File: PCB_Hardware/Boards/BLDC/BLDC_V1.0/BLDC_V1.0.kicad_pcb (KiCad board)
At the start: 4 copper layers, 0 parts

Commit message: Created organization around the symbol lib and did a first pass layout of the BDLC
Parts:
- added C1: 100n, Capacitor_SMD:C_0402_1005Metric, B.Cu at (191.8, 98.6)
- added C11: 33n, Capacitor_SMD:C_0402_1005Metric, B.Cu at (172.3, 99.6)
- added C12: 1u, Capacitor_SMD:C_0603_1608Metric, F.Cu at (181.4, 90.2)
- added C13: 100n, Capacitor_SMD:C_0402_1005Metric, F.Cu at (175.8, 90.4)
- added C14: 10u, Capacitor_SMD:C_0603_1608Metric, F.Cu at (177.4, 115.6)
- added C15: 1u, Capacitor_SMD:C_0603_1608Metric, F.Cu at (194.4, 97.0)
- added C16: 47n, Capacitor_SMD:C_0805_2012Metric, F.Cu at (191.0, 96.8)
- added C17: 100n, Capacitor_SMD:C_0402_1005Metric, F.Cu at (193.0, 94.8)
- added C18: 1u, Capacitor_SMD:C_0402_1005Metric, F.Cu at (189.6, 96.0)
- added C19: 1u, Capacitor_SMD:C_0402_1005Metric, F.Cu at (187.8, 96.2)
- added C2: 100n, Capacitor_SMD:C_0402_1005Metric, B.Cu at (167.0, 94.9)
- added C20: 1u, Capacitor_SMD:C_0402_1005Metric, F.Cu at (185.8, 84.5)
- added C21: 100n, Capacitor_SMD:C_0402_1005Metric, F.Cu at (186.5, 85.2)
- added C22: 2.2u, Capacitor_SMD:C_0805_2012Metric, F.Cu at (202.1, 88.5)
- added C23: 330u, Capacitor_THT:CP_Radial_D12.5mm_P5.00mm, F.Cu at (193.0, 107.6)
- added C24: 10u, Capacitor_SMD:C_0603_1608Metric, B.Cu at (168.8, 107.0)
- added C25: 2.2u, Capacitor_SMD:C_0805_2012Metric, F.Cu at (202.3, 74.5)
- added C26: 2.2u, Capacitor_SMD:C_0805_2012Metric, F.Cu at (202.2, 102.2)
- added C28: 100n, Capacitor_SMD:C_0805_2012Metric, F.Cu at (185.4, 97.4)
- added C29: 100n, Capacitor_SMD:C_0402_1005Metric, B.Cu at (179.2, 84.8)
- added C3: 100n, Capacitor_SMD:C_0402_1005Metric, F.Cu at (167.0, 85.9)
- added C30: 4.7u, Capacitor_SMD:C_0603_1608Metric, B.Cu at (203.8, 80.2)
- added C31: 100n, Capacitor_SMD:C_0402_1005Metric, B.Cu at (203.0, 77.6)
- added C32: 100n, Capacitor_SMD:C_0402_1005Metric, B.Cu at (192.8, 71.8)
- added C33: 100n, Capacitor_SMD:C_0402_1005Metric, B.Cu at (187.0, 82.4)
- added C34: 100n, Capacitor_SMD:C_0402_1005Metric, B.Cu at (190.0, 88.8)
- added C35: 100n, Capacitor_SMD:C_0402_1005Metric, B.Cu at (196.2, 88.2)
- added C36: 100n, Capacitor_SMD:C_0402_1005Metric, B.Cu at (191.0, 73.6)
- added C37: 4.7u, Capacitor_SMD:C_0603_1608Metric, F.Cu at (199.8, 70.2)
- added C38: 100n, Capacitor_SMD:C_0402_1005Metric, F.Cu at (207.6, 72.4)
- added C39: 10u, Capacitor_SMD:C_0402_1005Metric, B.Cu at (190.0, 116.8)
- added C4: 47n, Capacitor_SMD:C_0402_1005Metric, F.Cu at (176.4, 86.8)
- added C40: 22u, Capacitor_SMD:C_0805_2012Metric, B.Cu at (187.3, 122.3)
- added C41: 22u, Capacitor_SMD:C_0805_2012Metric, F.Cu at (188.2, 113.5)
- added C42: 100n, Capacitor_SMD:C_0402_1005Metric, B.Cu at (190.2, 72.8)
- added C43: 18p, Capacitor_SMD:C_0402_1005Metric, B.Cu at (185.2, 89.9)
- added C44: 18p, Capacitor_SMD:C_0402_1005Metric, B.Cu at (185.2, 84.4)
- added C45: 100n, Capacitor_SMD:C_0402_1005Metric, B.Cu at (182.6, 91.0)
- added C46: 100n, Capacitor_SMD:C_0402_1005Metric, F.Cu at (201.2, 90.0)
- added C47: ?, Capacitor_SMD:C_0402_1005Metric, F.Cu at (193.4, 77.8)
- added C48: ?, Capacitor_SMD:C_0402_1005Metric, F.Cu at (195.6, 77.8)
- added C49: ?, Capacitor_SMD:C_0402_1005Metric, F.Cu at (197.8, 77.8)
- added C50: 2.2u, Capacitor_SMD:C_0805_2012Metric, B.Cu at (168.8, 117.4)
- added C51: 2.2n, Capacitor_SMD:C_0402_1005Metric, B.Cu at (178.2, 121.2)
- added C52: 3.3n, Capacitor_SMD:C_0402_1005Metric, B.Cu at (181.2, 121.2)
- added C53: 56p, Capacitor_SMD:C_0402_1005Metric, B.Cu at (182.4, 121.2)
- added C54: 22u, Capacitor_SMD:C_0805_2012Metric, B.Cu at (184.2, 116.4)
- added C57: 100n, Capacitor_SMD:C_0402_1005Metric, B.Cu at (212.2, 122.2)
- added D1: SD05T1G, Diode_SMD:D_SOD-323, B.Cu at (194.0, 97.4)
- added D10: SMAJ5.0A, Diode_SMD:D_SMA, B.Cu at (196.8, 66.0)
- added D11: RED, LED_SMD:LED_0603_1608Metric, F.Cu at (218.4, 115.6)
- added D12: RED, LED_SMD:LED_0603_1608Metric, F.Cu at (218.4, 113.8)
- added D13: RED, LED_SMD:LED_0603_1608Metric, F.Cu at (171.8, 85.6)
- added D14: PESD5V0L1UL, Diode_SMD:D_SOD-882, B.Cu at (197.6, 68.6)
- added D15: SMCJ90A, Diode_SMD:D_SMC, B.Cu at (207.8, 105.8)
- added D16: SMCJ90A, Diode_SMD:D_SMC, B.Cu at (207.8, 99.0)
- added D17: SMCJ90A, Diode_SMD:D_SMC, B.Cu at (214.8, 75.1)
- added D18: BZG05C75-M3-08, Diode_SMD:D_SMA, B.Cu at (166.1, 109.0)
- added D19: PESD5V0L1UL, Diode_SMD:D_SOD-882, F.Cu at (168.8, 71.3)
- added D2: PESD1CAN, Package_TO_SOT_SMD:SOT-23, F.Cu at (176.4, 78.8)
- added D20: PESD5V0L1UL, Diode_SMD:D_SOD-882, F.Cu at (170.2, 71.3)
- added D21: RED, LED_SMD:LED_0603_1608Metric, F.Cu at (168.2, 122.2)
- added D22: PESD5V0S1UL, Diode_SMD:D_SOD-882, B.Cu at (209.8, 122.0)
- added D23: PESD3V3S1UL, Diode_SMD:D_SOD-882, B.Cu at (207.2, 122.0)
- added D24: PESD5V0S1UL, Diode_SMD:D_SOD-882, B.Cu at (204.8, 122.0)
- added D3: PESD1CAN, Package_TO_SOT_SMD:SOT-23, B.Cu at (173.0, 80.8)
- added D4: SMCJ78A, Diode_SMD:D_SMC, F.Cu at (174.0, 120.0)
- added D5: SS10150, Diode_SMD:D_SOD-123F, B.Cu at (196.0, 113.8)
- added D6: PESD3V3S1UL, Diode_SMD:D_SOD-882, B.Cu at (181.4, 70.0)
- added D7: PESD5V0L1UL, Diode_SMD:D_SOD-882, B.Cu at (185.8, 73.8)
- added D8: PESD3V3S1UL, Diode_SMD:D_SOD-882, B.Cu at (182.0, 72.0)
- added D9: PESD3V3S1UL, Diode_SMD:D_SOD-882, B.Cu at (176.6, 70.0)
- added F1: MF-PSMF050X-2, Fuse:Fuse_0805_2012Metric, B.Cu at (185.8, 76.4)
- added F2: MF-PSMF050X-2, Fuse:Fuse_0805_2012Metric, B.Cu at (184.0, 71.0)
- added F3: MF-PSMF050X-2, Fuse:Fuse_0805_2012Metric, F.Cu at (169.4, 65.4)
- added F4: MF-PSMF050X-2, Fuse:Fuse_0805_2012Metric, F.Cu at (195.0, 71.4)
- added F5: MF-PSMF050X-2, Fuse:Fuse_0805_2012Metric, B.Cu at (186.6, 68.8)
- added F6: MF-PSMF050X-2, Fuse:Fuse_1812_4532Metric, B.Cu at (201.4, 115.4)
- added H1: MountingHole, MountingHole:MountingHole_3.2mm_M3, F.Cu at (164.0, 68.0)
- added H2: MountingHole, MountingHole:MountingHole_3.2mm_M3, F.Cu at (164.0, 120.0)
- added H3: MountingHole, MountingHole:MountingHole_3.2mm_M3, F.Cu at (216.0, 120.0)
- added H4: MountingHole, MountingHole:MountingHole_3.2mm_M3, F.Cu at (216.0, 68.0)
- added H5: MountingHole_Pad, MountingHole:MountingHole_3.2mm_M3_DIN965_Pad, F.Cu at (216.2, 105.9)
- added H6: MountingHole_Pad, MountingHole:MountingHole_3.2mm_M3_DIN965_Pad, F.Cu at (215.9, 94.2)
- added H7: MountingHole_Pad, MountingHole:MountingHole_3.2mm_M3_DIN965_Pad, F.Cu at (215.7, 82.3)
- added J1: Conn_01x04_Pin, DBRobot:CONN_JST_SM04B-PASS, B.Cu at (165.0, 78.8)
- added J11: GT-USB-7010ASV, Connector_USB:USB_C_Receptacle_G-Switch_GT-USB-7010ASV, F.Cu at (206.0, 67.0)
- added J14: 47053-1000, Connector:FanPinHeader_1x04_P2.54mm_Vertical, F.Cu at (202.2, 119.7)
- added J2: Conn_01x04_Pin, DBRobot:CONN_JST_SM04B-PASS, F.Cu at (165.0, 78.8)
- added J3: Conn_01x02_Pin, Connector_AMASS:AMASS_XT30PW-M_1x02_P2.50mm_Horizontal, F.Cu at (173.0, 106.5)
- added J4: Conn_01x02_Pin, Connector_AMASS:AMASS_XT30PW-M_1x02_P2.50mm_Horizontal, F.Cu at (173.0, 91.2)
- added J5: Conn_01x02_Socket, Connector_JST:JST_XH_S2B-XH-A-1_1x02_P2.50mm_Horizontal, F.Cu at (194.8, 116.2)
- added J6: Conn_01x02_Socket, Connector_JST:JST_GH_SM02B-GHS-TB_1x02-1MP_P1.25mm_Horizontal, B.Cu at (179.0, 67.0)
- added J7: Conn_ARM_SWD_TagConnect_TC2030, Connector:Tag-Connect_TC2030-IDC-FP_2x03_P1.27mm_Vertical, F.Cu at (180.5, 96.2)
- added J8: Conn_02x06_Odd_Even, Connector_JST:JST_PUD_S12B-PUDSS-1_2x06_P2.00mm_Horizontal, F.Cu at (184.0, 75.8)
- added J9: Conn_01x06_Socket, Connector_JST:JST_GH_SM06B-GHS-TB_1x06-1MP_P1.25mm_Horizontal, F.Cu at (193.0, 67.0)
- added L1: 68u SRN5040TA-680K, Inductor_SMD:L_Sunlord_SWPA4020S, B.Cu at (180.6, 117.8)
- added Q1: SI2302, Package_TO_SOT_SMD:SOT-23, F.Cu at (173.8, 81.8)
- added Q10: BC847, Package_TO_SOT_SMD:SOT-23, B.Cu at (190.2, 120.4)
- added Q11: BSS138, Package_TO_SOT_SMD:SOT-23, B.Cu at (211.4, 117.4)
- added Q12: BSS84, Package_TO_SOT_SMD:SOT-23, B.Cu at (180.6, 79.4)
- added Q13: IPT015N10N5, Package_TO_SOT_SMD:Infineon_PG-HSOF-8-1, B.Cu at (181.0, 107.6)
- added Q14: SI2302, Package_TO_SOT_SMD:SOT-23, B.Cu at (169.6, 69.4)
- added Q2: IPT015N10N5, Package_TO_SOT_SMD:Infineon_PG-HSOF-8-1, F.Cu at (181.0, 107.5)
- added Q3: TPH3R70APL, DBRobot:SOP AdvanceN_TOS, F.Cu at (208.3, 104.4)
- added Q4: TPH3R70APL, DBRobot:SOP AdvanceN_TOS, F.Cu at (208.3, 111.4)
- added Q5: TPH3R70APL, DBRobot:SOP AdvanceN_TOS, F.Cu at (208.3, 90.5)
- added Q6: TPH3R70APL, DBRobot:SOP AdvanceN_TOS, F.Cu at (208.3, 97.5)
- added Q7: TPH3R70APL, DBRobot:SOP AdvanceN_TOS, F.Cu at (208.4, 76.5)
- added Q8: TPH3R70APL, DBRobot:SOP AdvanceN_TOS, F.Cu at (208.4, 83.4)
- added Q9: TPH3R70APL, DBRobot:SOP AdvanceN_TOS, B.Cu at (197.2, 120.6)
- added R1: 60, Resistor_SMD:R_0805_2012Metric, F.Cu at (176.6, 82.4)
- added R10: 3.9k, Resistor_SMD:R_0805_2012Metric, B.Cu at (170.1, 98.3)
- added R11: 3.9k, Resistor_SMD:R_0402_1005Metric, B.Cu at (176.0, 99.5)
- added R12: 1m, Resistor_SMD:R_2512_6332Metric, F.Cu at (202.4, 107.2)
- added R13: 1m, Resistor_SMD:R_2512_6332Metric, F.Cu at (202.3, 94.4)
- added R14: 1m, Resistor_SMD:R_2512_6332Metric, F.Cu at (202.1, 79.6)
- added R15: 1k, Resistor_SMD:R_0402_1005Metric, F.Cu at (186.6, 81.9)
- added R16: 1k, Resistor_SMD:R_0402_1005Metric, F.Cu at (188.3, 79.7)
- added R17: 100k, Resistor_SMD:R_0603_1608Metric, B.Cu at (177.0, 86.2)
- added R18: 10k, Resistor_SMD:R_0402_1005Metric, B.Cu at (187.6, 120.2)
- added R19: 4.7, Resistor_SMD:R_0402_1005Metric, B.Cu at (190.2, 122.8)
- added R2: 60, Resistor_SMD:R_0805_2012Metric, F.Cu at (175.8, 85.2)
- added R20: 1k, Resistor_SMD:R_0402_1005Metric, B.Cu at (188.8, 118.8)
- added R21: 4.7k, Resistor_SMD:R_0603_1608Metric, B.Cu at (177.0, 84.6)
- added R22: 10k, Resistor_SMD:R_0402_1005Metric, B.Cu at (209.0, 94.0)
- added R23: 10k, Resistor_SMD:R_0402_1005Metric, B.Cu at (179.4, 70.8)
- added R24: 0, Resistor_SMD:R_0402_1005Metric, B.Cu at (187.6, 87.8)
- added R25: 4.7k, Resistor_SMD:R_0402_1005Metric, B.Cu at (176.0, 78.0)
- added R26: 4.7k, Resistor_SMD:R_0402_1005Metric, B.Cu at (178.0, 78.0)
- added R27: 4.7k, Resistor_SMD:R_0402_1005Metric, F.Cu at (195.0, 84.4)
- added R28: 4.7k, Resistor_SMD:R_0402_1005Metric, F.Cu at (199.6, 89.2)
- added R29: 49, Resistor_SMD:R_0805_2012Metric, B.Cu at (166.1, 103.3)
- added R30: 24.9k, Resistor_SMD:R_0402_1005Metric, B.Cu at (170.8, 116.0)
- added R31: 121k, Resistor_SMD:R_0402_1005Metric, B.Cu at (180.0, 121.2)
- added R32: 0, Resistor_SMD:R_0402_1005Metric, F.Cu at (196.7, 77.8)
- added R33: 1.8k, Resistor_SMD:R_0402_1005Metric, F.Cu at (167.4, 71.1)
- added R34: 3.3k, Resistor_SMD:R_0402_1005Metric, F.Cu at (168.2, 68.6)
- added R35: 10k, Resistor_SMD:R_0402_1005Metric, B.Cu at (168.0, 67.8)
- added R36: 1k, Resistor_SMD:R_0402_1005Metric, B.Cu at (167.4, 71.1)
- added R37: 0, Resistor_SMD:R_0402_1005Metric, F.Cu at (194.5, 77.8)
- added R38: 0, Resistor_SMD:R_0402_1005Metric, F.Cu at (192.3, 77.8)
- added R39: 453k, Resistor_SMD:R_0402_1005Metric, B.Cu at (177.0, 116.0)
- added R40: 143k, Resistor_SMD:R_0402_1005Metric, B.Cu at (175.0, 116.0)
- added R47: 5.1k, Resistor_SMD:R_0402_1005Metric, B.Cu at (208.4, 68.2)
- added R48: 5.1k, Resistor_SMD:R_0402_1005Metric, B.Cu at (203.6, 68.2)
- added R49: 100k, Resistor_SMD:R_0402_1005Metric, B.Cu at (191.4, 117.7)
- added R50: 5k, Resistor_SMD:R_0402_1005Metric, B.Cu at (219.0, 117.0)
- added R51: 2.2k, Resistor_SMD:R_0402_1005Metric, B.Cu at (218.4, 113.8)
- added R52: 100k, Resistor_SMD:R_0402_1005Metric, B.Cu at (193.2, 116.0)
- added R53: 100k, Resistor_SMD:R_0402_1005Metric, B.Cu at (187.6, 113.8)
- added R54: 100k, Resistor_SMD:R_0402_1005Metric, B.Cu at (193.2, 114.0)
- added R55: 2.2k, Resistor_SMD:R_0402_1005Metric, F.Cu at (169.9, 85.9)
- added R56: 100, Resistor_SMD:R_0402_1005Metric, B.Cu at (208.8, 115.8)
- added R57: 100k, Resistor_SMD:R_0402_1005Metric, B.Cu at (209.0, 117.4)
- added R58: 10k, Resistor_SMD:R_0402_1005Metric, B.Cu at (211.2, 122.2)
- added R59: 10k, Resistor_SMD:R_0402_1005Metric, B.Cu at (205.4, 116.6)
- added R6: 0.5m, Resistor_SMD:R_2512_6332Metric, F.Cu at (181.4, 119.4)
- added R60: 1k, Resistor_SMD:R_0402_1005Metric, B.Cu at (205.4, 117.8)
- added R61: 2.2k, Resistor_SMD:R_0402_1005Metric, B.Cu at (168.2, 122.2)
- added R7: 102k, Resistor_SMD:R_0805_2012Metric, B.Cu at (166.0, 99.0)
- added R8: 30k, Resistor_SMD:R_0805_2012Metric, B.Cu at (163.2, 101.2)
- added R9: 113k, Resistor_SMD:R_0805_2012Metric, B.Cu at (168.0, 99.0)
- added TH1: Thermistor, Resistor_SMD:R_0603_1608Metric, B.Cu at (207.6, 94.0)
- added U1: DRV8353SRTAR, Package_DFN_QFN:QFN-40-1EP_6x6mm_P0.5mm_EP4.6x4.6mm, F.Cu at (190.4, 90.6)
- added U10: TPD2E2U06DCK, Package_TO_SOT_SMD:SOT-323_SC-70, B.Cu at (206.1, 65.6)
- added U11: AMS1117-3.3, Package_TO_SOT_SMD:SOT-223-3_TabPin2, F.Cu at (187.3, 119.1)
- added U12: LM66100DCK, Package_TO_SOT_SMD:SOT-363_SC-70-6, B.Cu at (187.3, 115.6)
- added U13: LM66100DCK, Package_TO_SOT_SMD:SOT-363_SC-70-6, B.Cu at (191.5, 114.2)
- added U14: SRV05-4, Package_TO_SOT_SMD:SOT-23-6, F.Cu at (188.8, 72.0)
- added U15: TS5A3159ADBVR, Package_TO_SOT_SMD:SOT-23-6, B.Cu at (189.8, 66.4)
- added U16: CAT24C512C8UTR, DBRobot:CAT24C512C8UTR, B.Cu at (200.3, 86.8)
- added U2: MT6835GT-STD, Package_SO:TSSOP-16_4.4x5mm_P0.65mm, B.Cu at (190.1, 94.0)
- added U3: TCAN1044VDR, Package_SO:SOIC-8_3.9x4.9mm_P1.27mm, B.Cu at (167.0, 90.6)
- added U4: ~, Package_SO:SOIC-8-1EP_3.9x4.9mm_P1.27mm_EP2.29x3mm, B.Cu at (173.8, 119.3)
- added U5: LM5069MM-2, Package_SO:MSOP-10_3x3mm_P0.5mm, B.Cu at (172.2, 101.9)
- added U6: TLV70233_SOT23-5, Package_TO_SOT_SMD:SOT-23-5, F.Cu at (178.4, 89.8)
- added U7: STM32G474RET6, Package_QFP:LQFP-64_10x10mm_P0.5mm, B.Cu at (195.0, 80.0)
- added U8: SRV05-4, Package_TO_SOT_SMD:SOT-23-6, F.Cu at (182.8, 78.8)
- added U9: SRV05-4, Package_TO_SOT_SMD:SOT-23-6, B.Cu at (173.6, 70.6)
- added Y2: XXGBBCNANF-25.000000MHZ, Crystal:Crystal_SMD_3225-4Pin_3.2x2.5mm, B.Cu at (185.2, 87.2)
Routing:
- net GND: track 0.00 -> 205.9 mm, vias 0 -> 91
- net +5V: track 0.00 -> 176.9 mm, vias 0 -> 6
- net /Break R/BREAK_R: track 0.00 -> 127.4 mm, vias 0 -> 11
- net /OR Inputs/5V_USB: track 0.00 -> 103.8 mm, vias 0 -> 6
- net +3.3V: track 0.00 -> 81.6 mm, vias 0 -> 18
- net +BATT: track 0.00 -> 77.6 mm, vias 0 -> 66
- net /Encoder/ENCODER_MOSI: track 0.00 -> 70.5 mm, vias 0 -> 2
- net /Encoder/ENCODER_MISO: track 0.00 -> 64.0 mm, vias 0 -> 4
- net /CANFD/CAN-: track 0.00 -> 60.9 mm, vias 0 -> 2
- net /CANFD/CAN+: track 0.00 -> 58.7 mm, vias 0 -> 2
- net /MCU/SWDIO: track 0.00 -> 47.8 mm, vias 0 -> 4
- net /GPIO/AUX2_V_CRTL: track 0.00 -> 46.4 mm, vias 0 -> 3
- net +3.3VA: track 0.00 -> 46.4 mm, vias 0 -> 3
- net /GPIO/PA8/SDA: track 0.00 -> 44.8 mm, vias 0 -> 1
- net /Fan/TACH: track 0.00 -> 44.8 mm, vias 0 -> 2
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- added copper zone on F.Cu, net +12-60V
- added copper zone on In2.Cu, net +3.3V
- added copper zone on B.Cu, net +BATT
- added copper zone on In2.Cu, net +BATT
- added copper zone on In1.Cu, net GND
- added copper zone on B.Cu, net Net-(D15-K)
- added copper zone on F.Cu, net Net-(D15-K)
- added copper zone on B.Cu, net Net-(D16-K)
- added copper zone on F.Cu, net Net-(D16-K)
- added copper zone on B.Cu, net Net-(D17-K)
- added copper zone on F.Cu, net Net-(D17-K)
- added copper zone on B.Cu, net Net-(D18-K)
- added copper zone on B.Cu, net Net-(Q13-S)
- added copper zone on F.Cu, net Net-(Q13-S)
- added copper zone on F.Cu, net Net-(Q2-D)
- added copper zone on F.Cu, net Net-(U1-SPA)
- added copper zone on F.Cu, net Net-(U1-SPB)
- added copper zone on F.Cu, net Net-(U1-SPC)
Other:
- board outline added: 60 x 60 mm

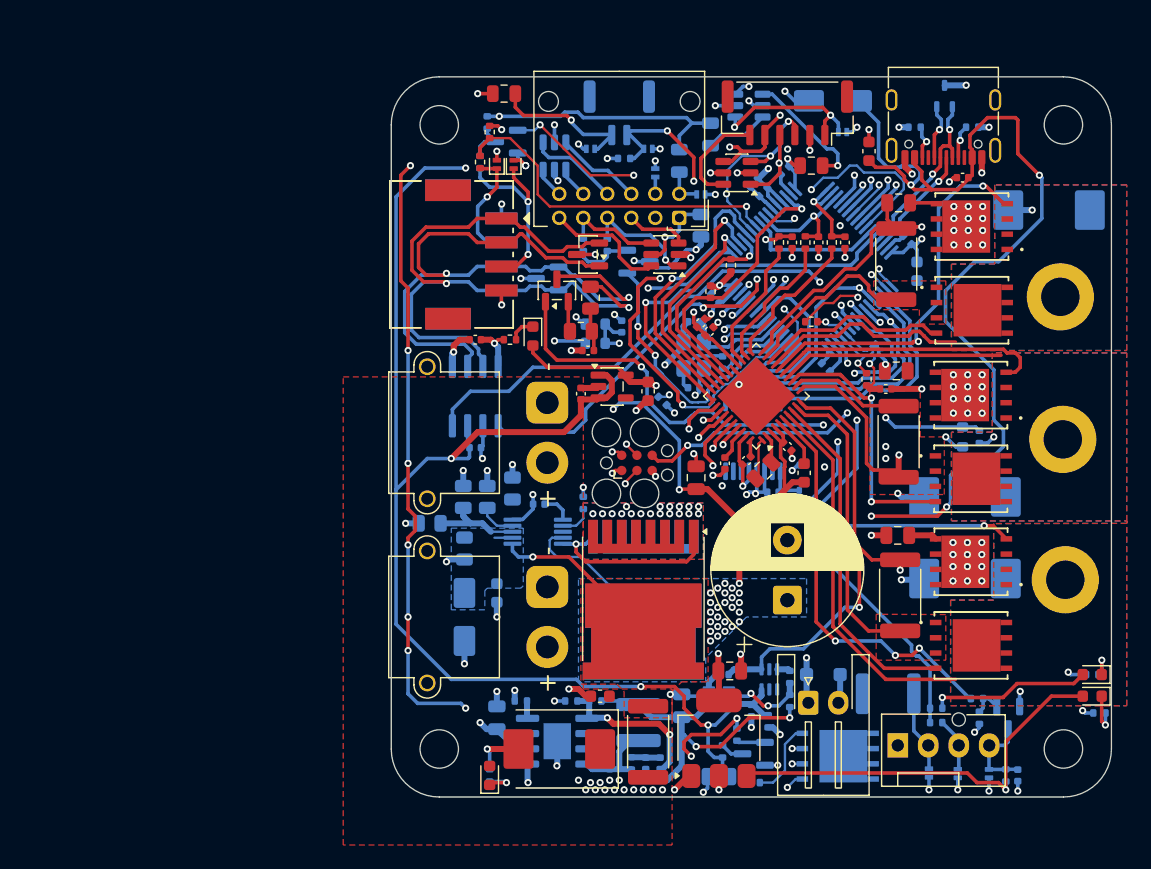
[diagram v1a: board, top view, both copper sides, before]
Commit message: complete redo of the BLDC layout
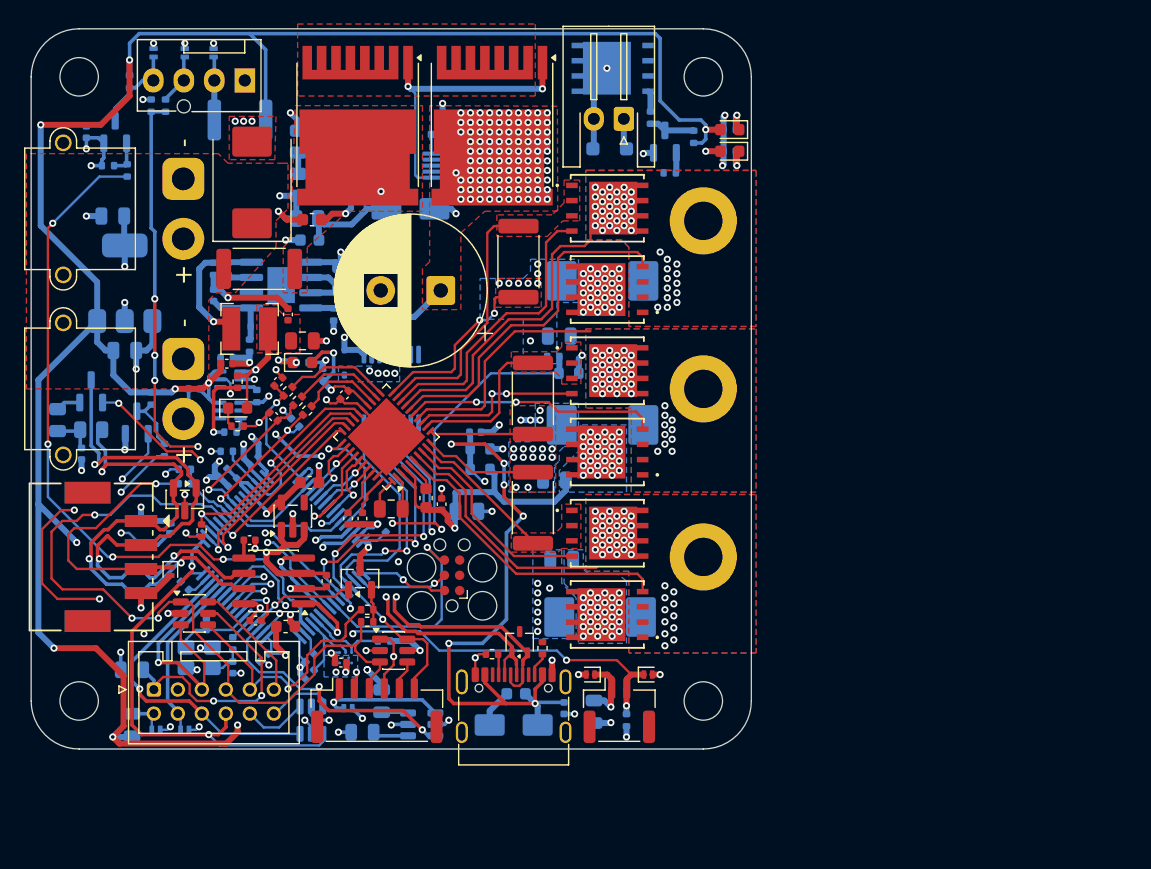
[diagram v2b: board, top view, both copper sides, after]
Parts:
- removed D3: PESD1CAN, Package_TO_SOT_SMD:SOT-23
- C13, C20, C22, C25, C26, C28, C37, C38, C4, C41, C47, D20, F3, F4, J2, Q1, R1, R15, R2, R27, R28, R33, R34, R55, U11: moved to B.Cu
- C2, C30, C39, C45, C52, C54, D6, D9, J1, J6, Q12, Q13, R25, R26, R47, R48, R52, R61, U10, U3: moved to F.Cu
- J8: footprint Connector_JST:JST_PUD_S12B-PUDSS-1_2x06_P2.00mm_Horizontal -> Connector_JST:JST_PUD_B12B-PUDSS_2x06_P2.00mm_Vertical
- L1: value 68u SRN5040TA-680K -> 68u SRN4018-680M; footprint Inductor_SMD:L_Sunlord_SWPA4020S -> Inductor_SMD:L_Bourns-SRN4018; moved to F.Cu
- moved C57 94.3 mm to (134.6, 68.6)
- moved R58 93.1 mm to (138.2, 64.4), turned to 90 degrees
- moved D22 91.9 mm to (140.2, 62.0), turned to 90 degrees
- moved Q11 89.0 mm to (137.0, 68.6), turned to 90 degrees
- moved D23 88.1 mm to (142.8, 62.0), turned to 90 degrees
- moved R57 85.9 mm to (136.4, 71.4), turned to 0 degrees
- moved D24 84.6 mm to (145.2, 62.0), turned to 90 degrees
- moved R56 83.4 mm to (138.0, 71.8), turned to 90 degrees
- moved R59 82.4 mm to (140.0, 66.4), turned to 90 degrees
- moved R60 82.2 mm to (141.2, 66.4), turned to -90 degrees
- moved H3 82.1 mm to (134.0, 116.0)
- moved J14 77.6 mm to (147.8, 64.3), turned to 180 degrees
- moved F6 72.1 mm to (147.4, 67.6), turned to 180 degrees
- moved F2 65.5 mm to (138.4, 118.0), turned to 90 degrees
- moved C41 63.9 mm to (136.8, 75.6), turned to 180 degrees
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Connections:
- J7 pad 3: /MCU/NRST -> unconnected-(J7-~{RESET}-Pad3)
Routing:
- net /Break R/BREAK_R: track 127.4 -> 0.00 mm, vias 11 -> 0
- net +5V: track 176.9 -> 225.2 mm, vias 6 -> 12
- net /MCU/SWDIO: track 47.8 -> 7.36 mm, vias 4 -> 1
- net /MCU/SWCLK: track 43.8 -> 7.85 mm, vias 4 -> 1
- net /CANFD/CANFD_RX: track 41.7 -> 7.67 mm, vias 2 -> 1
- net /MCU/INLB: track 39.8 -> 5.93 mm, vias 2 -> 1
- net /OR Inputs/5V_USB: track 103.8 -> 70.1 mm, vias 6 -> 9
- net /Encoder/ENCODER_MISO: track 64.0 -> 30.6 mm, vias 4 -> 2
- net /CANFD/CANFD_TX: track 38.3 -> 6.24 mm, vias 3 -> 1
- net +BATT: track 77.6 -> 46.0 mm, vias 66 -> 188
- net /MCU/INHB: track 39.5 -> 8.30 mm, vias 2 -> 1
- net /GPIO/PC4/SCL/ADC: track 34.3 -> 64.6 mm, vias 4 -> 3
- net /MCU/INHC: track 34.3 -> 4.78 mm, vias 2 -> 1
- net GND: track 205.9 -> 176.4 mm, vias 91 -> 106
- net /Encoder/ENCODER_MOSI: track 70.5 -> 41.1 mm, vias 2 -> 4
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- added copper zone on F.Cu, net +BATT
- added copper zone on F.Cu, net /OR Inputs/+5V MAIN
- added copper zone on B.Cu, net GND
- added copper zone on F.Cu, net GND
- removed copper zone on B.Cu, net Net-(D18-K)
- removed copper zone on B.Cu, net Net-(Q13-S)

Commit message: layout revision of the BLDC
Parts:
- moved C43 0.20 mm to (146.8, 113.4)
- moved F5 0.20 mm to (159.2, 115.8)
- moved R24 0.20 mm to (146.8, 111.4)
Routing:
- net /Break R/BREAK_R: track 0.00 -> 63.1 mm, vias 0 -> 5
- net /Encoder/ENCODER_MISO: track 30.6 -> 70.0 mm, vias 2 -> 6
- net /Encoder/ENCODER_MOSI: track 41.1 -> 56.7 mm, vias 4 -> 5
- net /Encoder/ENCODER_SCLK: track 42.9 -> 56.3 mm, vias 3 -> 4
- net GND: track 176.4 -> 189.4 mm, vias 106 -> 115
- net +3.3V: track 53.5 -> 58.0 mm, vias 20 -> 23
- net Net-(D22-K): track 7.44 -> 10.6 mm
- net /OR Inputs/+5V MAIN: track 9.60 -> 12.6 mm, vias 1 -> 2
- net /MCU/DRIVER_MOSI: track 18.0 -> 18.6 mm
- net /MCU/DRIVER_CSN: track 14.2 -> 14.8 mm
- net /MCU/DRIVER_SCLK: track 17.4 -> 17.9 mm
- net +5V: vias 12 -> 11
